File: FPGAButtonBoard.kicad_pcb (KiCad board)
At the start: 2 copper layers, 121.3 x 83.2 mm, 66 parts, among them J1 Conn_02x20_Odd_Even, J2 Analog Discovery 2, SW1 SW_DIP_x08, SW2 SW_DIP_x08, SW3 SW_Push, SW4 SW_Push, SW5 SW_Push, SW6 SW_Push, SW7 SW_Push, SW8 SW_SPST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

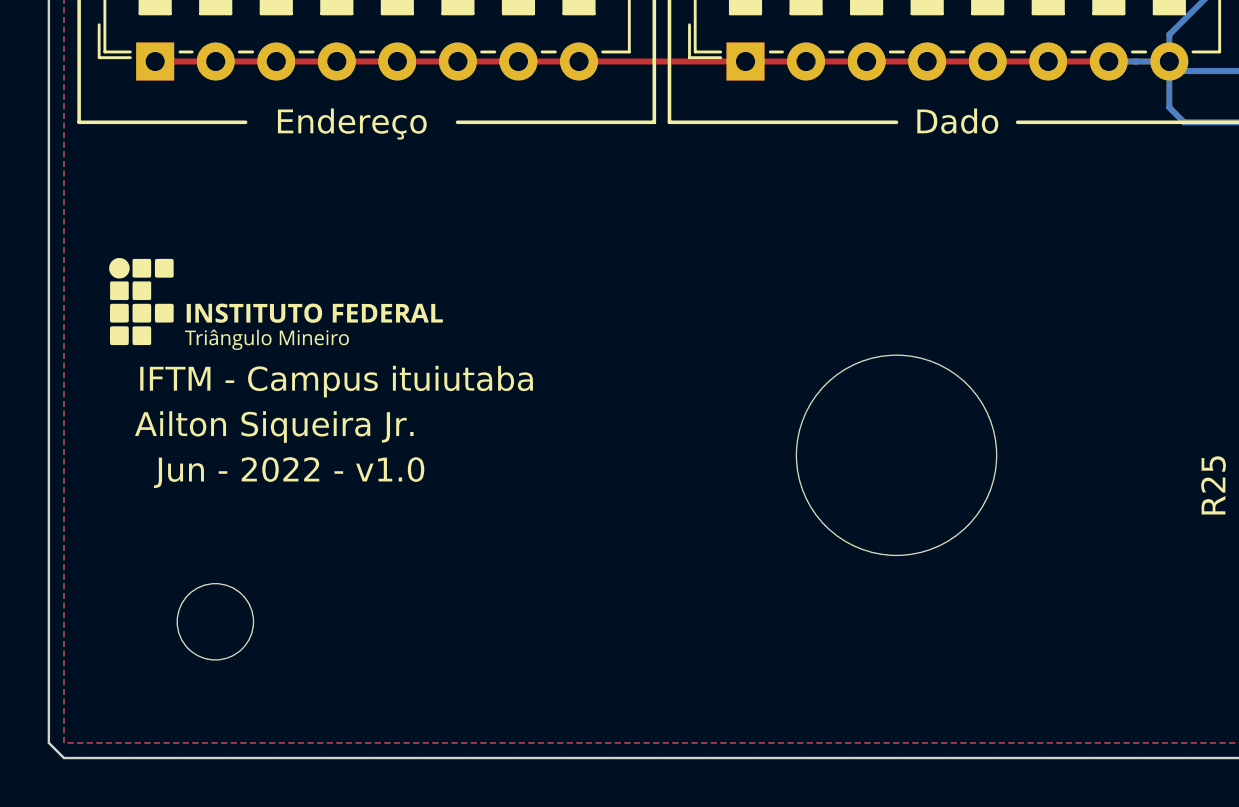
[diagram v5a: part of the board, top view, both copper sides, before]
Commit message: Adicionadas anotações dos pinos na placa.
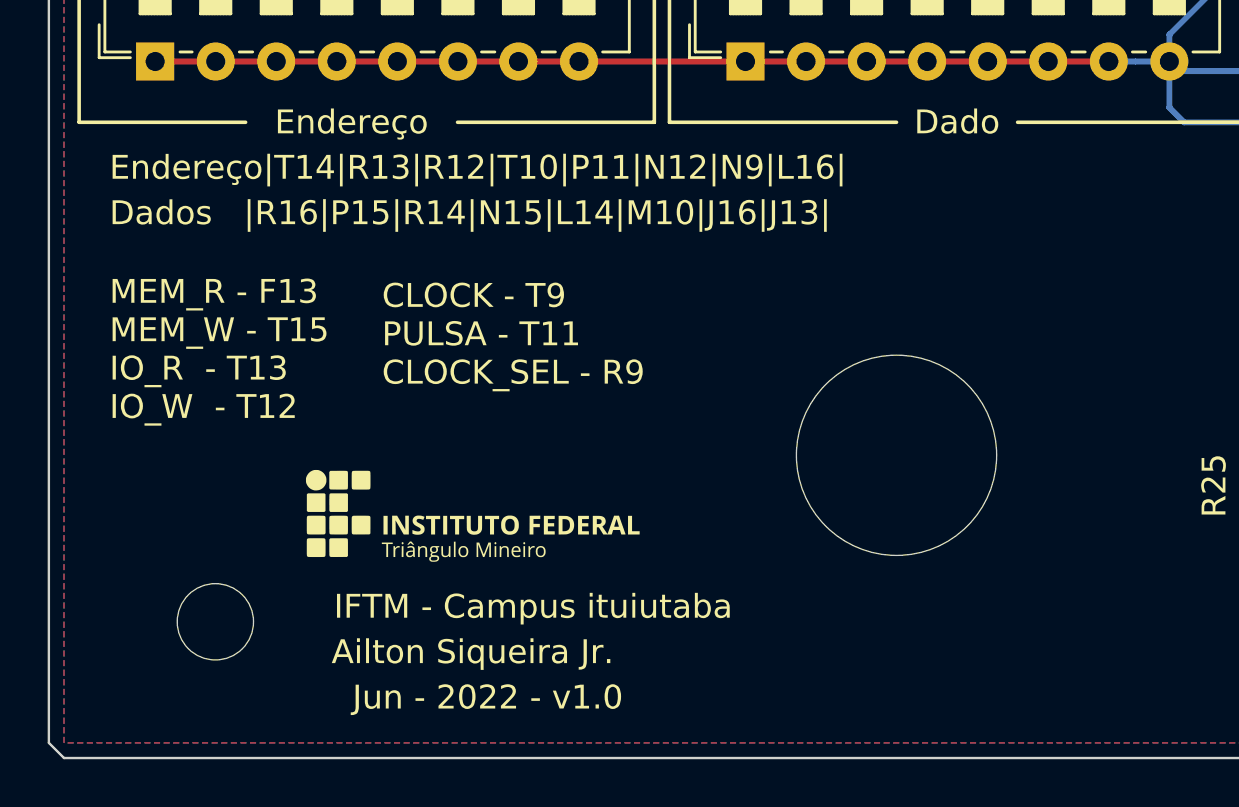
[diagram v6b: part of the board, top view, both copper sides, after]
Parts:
- moved G*** 12.1 mm to (108.0, 128.3)
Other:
- board text added: "CLOCK - T9 PULSA - T11 CLOCK_SEL - R9"
- board text added: "Dados |R16|P15|R14|N15|L14|M10|J16|J13|"
- board text added: "Endereço|T14|R13|R12|T10|P11|N12|N9|L16|"
- board text added: "MEM_R - F13 MEM_W - T15 IO_R - T13 IO_W - T12"
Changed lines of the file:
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@@
   )
   (footprint "Logo:IFTMLogoHor" (layer "F.Cu")
-    (at 99.695 119.38)
+    (at 107.95 128.27)
     (attr board_only exclude_from_pos_files exclude_from_bom)
     (fp_text reference "G***" (at 0 -2.54) (layer "F.SilkS") hide
@@
     (effects (font (size 1 1) (thickness 0.15)))
   )
-  (gr_text "Ailton Siqueira Jr." (at 99.695 124.46) (layer "F.SilkS")
+  (gr_text "Ailton Siqueira Jr." (at 107.95 133.985) (layer "F.SilkS")
     (effects (font (size 1 1) (thickness 0.15)))
+  )
+  (gr_text "Dados   |R16|P15|R14|N15|L14|M10|J16|J13|" (at 92.71 115.57) (layer "F.SilkS")
+    (effects (font (size 1 1) (thickness 0.15)) (justify left))
+  )
+  (gr_text "Endereço|T14|R13|R12|T10|P11|N12|N9|L16|" (at 92.71 113.665) (layer "F.SilkS")
+    (effects (font (size 1 1) (thickness 0.15)) (justify left))
   )
   (gr_text "MEM_R" (at 170.18 105.41) (layer "F.SilkS")
     (effects (font (size 1 1) (thickness 0.15)))
   )
-  (gr_text "Jun - 2022 - v1.0" (at 100.33 126.365) (layer "F.SilkS")
+  (gr_text "Jun - 2022 - v1.0" (at 108.585 135.89) (layer "F.SilkS")
     (effects (font (size 1 1) (thickness 0.15)))
   )
@@
     (effects (font (size 1 1) (thickness 0.15)))
   )
+  (gr_text "CLOCK - T9\nPULSA - T11\nCLOCK_SEL - R9" (at 104.14 120.65) (layer "F.SilkS")
+    (effects (font (size 1 1) (thickness 0.15)) (justify left))
+  )
   (gr_text "Pulsa" (at 193.04 134.62) (layer "F.SilkS")
     (effects (font (size 1 1) (thickness 0.15)))
+  )
+  (gr_text "MEM_R - F13\nMEM_W - T15\nIO_R  - T13\nIO_W  - T12\n" (at 92.71 121.285) (layer "F.SilkS")
+    (effects (font (size 1 1) (thickness 0.15)) (justify left))
   )
   (gr_text "Ajuste de Freq." (at 175.895 135.89) (layer "F.SilkS")
     (effects (font (size 1 1) (thickness 0.15)))
   )
-  (gr_text "IFTM - Campus ituiutaba" (at 102.235 122.555) (layer "F.SilkS")
+  (gr_text "IFTM - Campus ituiutaba" (at 110.49 132.08) (layer "F.SilkS")
     (effects (font (size 1 1) (thickness 0.15)))
   )

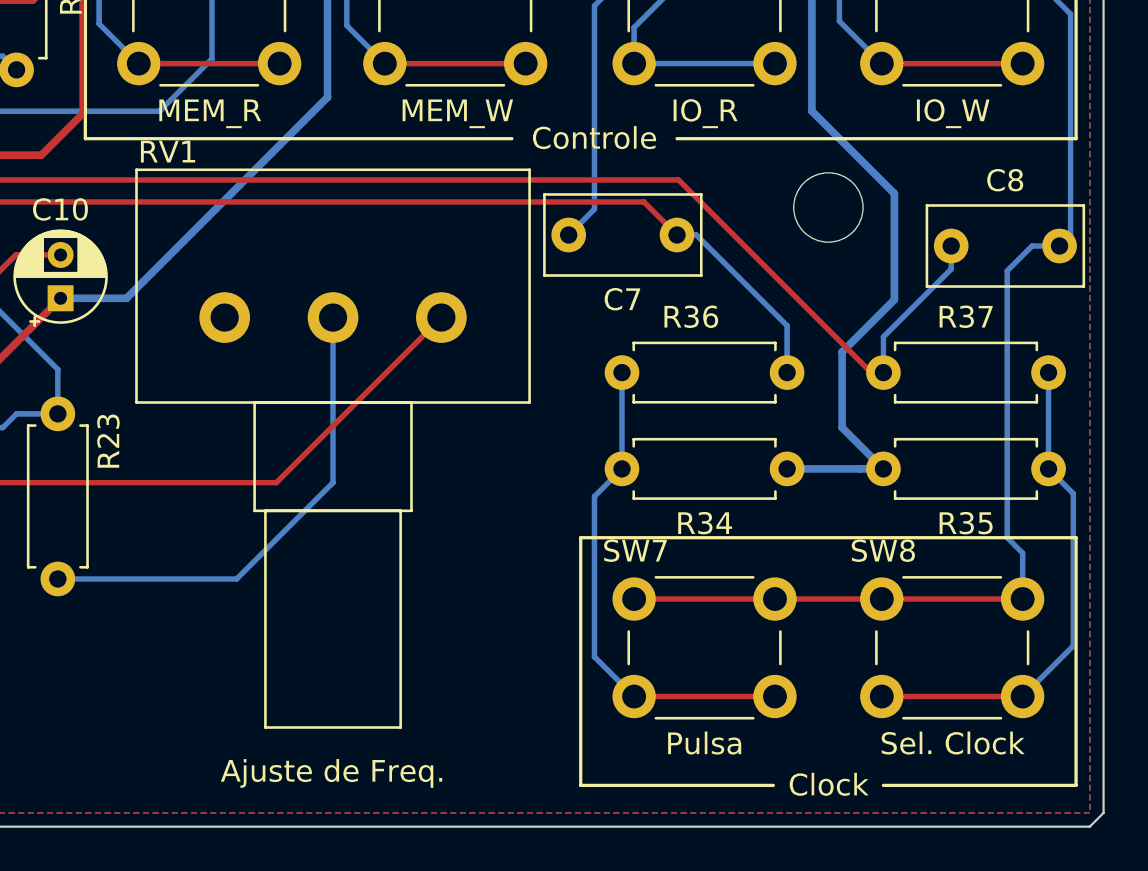
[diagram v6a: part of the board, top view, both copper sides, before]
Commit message: Corrigido o botão de seleção de Clock e valores dos capacitores.
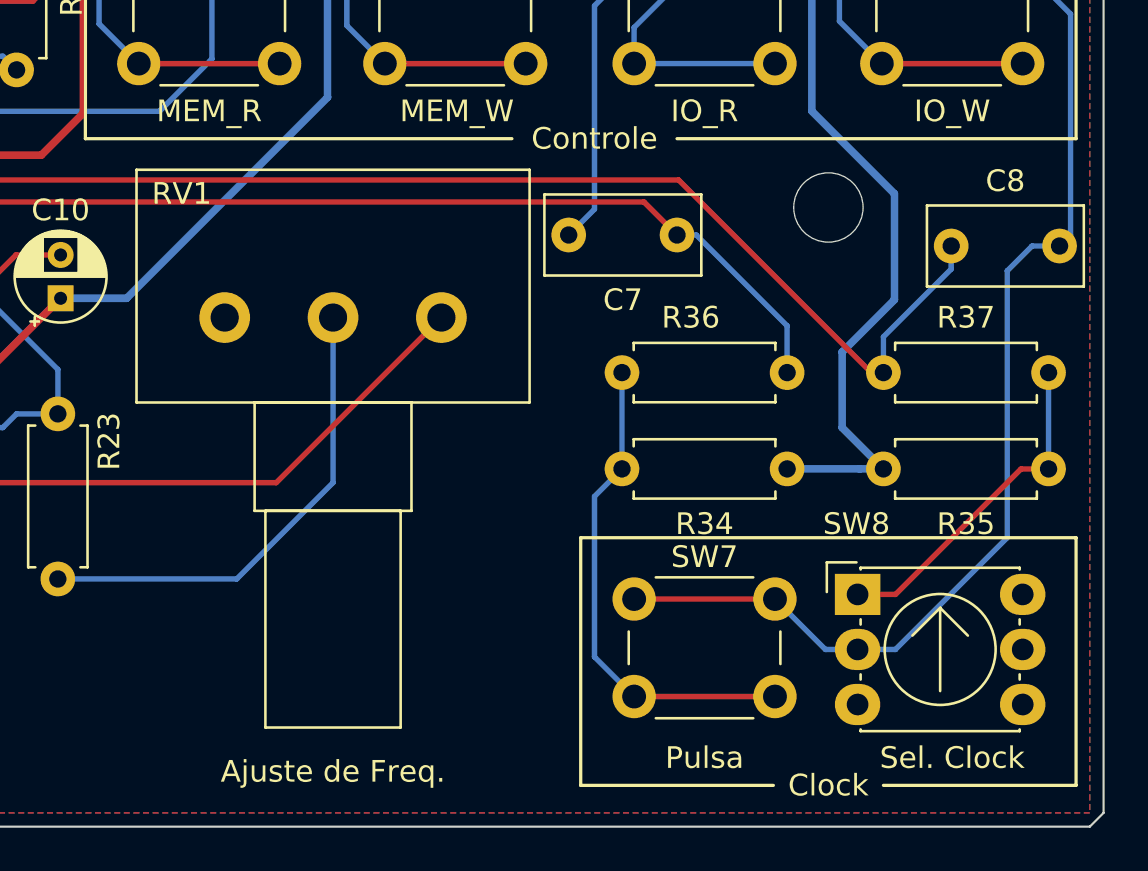
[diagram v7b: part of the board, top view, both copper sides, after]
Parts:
- C3, C4, C5, C6, C7, C8: value 100nF -> 47nF
- SW8: value SW_SPST -> SW_Push_DPDT; footprint Button_Switch_THT:SW_PUSH_6mm -> Logo:Nidec_Copal_SH-7010C_Mod
- moved SW8 1.14 mm to (200.1, 127.7)
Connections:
- SW8 pad 1: GND -> /DebounceCircuit3/SW_IN_6
- SW8 pad 2: /DebounceCircuit3/SW_IN_6 -> GND
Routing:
- net /DebounceCircuit3/SW_IN_6: track 22.9 -> 15.7 mm
- net GND: track 385.9 -> 385.1 mm

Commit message: Atualizado os valores dos capacitores
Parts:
- C1: value 10uF -> 47uF
- C3, C4, C5, C6, C7, C8: value 47nF -> 100nF
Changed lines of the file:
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@@
       (layerselection 0x00010fc_ffffffff)
       (disableapertmacros false)
-      (usegerberextensions false)
+      (usegerberextensions true)
       (usegerberattributes true)
-      (usegerberadvancedattributes true)
-      (creategerberjobfile true)
+      (usegerberadvancedattributes false)
+      (creategerberjobfile false)
       (svguseinch false)
       (svgprecision 6)
@@
       (psa4output false)
       (plotreference true)
-      (plotvalue true)
+      (plotvalue false)
       (plotinvisibletext false)
       (sketchpadsonfab false)
-      (subtractmaskfromsilk false)
+      (subtractmaskfromsilk true)
       (outputformat 1)
       (mirror false)
-      (drillshape 1)
+      (drillshape 0)
       (scaleselection 1)
-      (outputdirectory "")
+      (outputdirectory "Gerber/")
     )
   )
@@
       (effects (font (size 1 1) (thickness 0.15)))
     )
-    (fp_text value "10uF" (at -1.5674 0) (layer "F.Fab")
+    (fp_text value "47uF" (at -1.5674 0) (layer "F.Fab")
       (effects (font (size 1 1) (thickness 0.15)))
     )
@@
       (effects (font (size 1 1) (thickness 0.15)))
     )
-    (fp_text value "47nF" (at 2.5 3) (layer "F.Fab")
+    (fp_text value "100nF" (at 2.5 3) (layer "F.Fab")
       (effects (font (size 1 1) (thickness 0.15)))
     )
@@
       (effects (font (size 1 1) (thickness 0.15)))
     )
-    (fp_text value "47nF" (at 2.5 3) (layer "F.Fab")
+    (fp_text value "100nF" (at 2.5 3) (layer "F.Fab")
       (effects (font (size 1 1) (thickness 0.15)))
     )
@@
       (effects (font (size 1 1) (thickness 0.15)))
     )
-    (fp_text value "47nF" (at 2.5 3) (layer "F.Fab")
+    (fp_text value "100nF" (at 2.5 3) (layer "F.Fab")
       (effects (font (size 1 1) (thickness 0.15)))
     )
@@
     (fp_line (start 5.72 -5.1) (end 5.72 40.66) (layer "F.Fab") (width 0.1))
     (fp_line (start -1.98 -3.91) (end 4.52 -3.91) (layer "F.Fab") (width 0.1))
-    (pad "1" thru_hole roundrect (at 0 0 90) (size 1.7 1.7) (drill 1) (layers *.Cu *.Mask) (roundrect_rratio 0.147059)
+    (pad "1" thru_hole roundrect (at 0 0 90) (size 1.7 1.7) (drill 1) (layers *.Cu *.Mask) (roundrect_rratio 0.1470588235)
       (net 30 "/D7") (pinfunction "Pin_1") (pintype "passive"))
     (pad "2" thru_hole circle (at 2.54 0 90) (size 1.7 1.7) (drill 1) (layers *.Cu *.Mask)
@@
       (effects (font (size 1 1) (thickness 0.15)))
     )
-    (fp_text value "47nF" (at 2.5 3 180) (layer "F.Fab")
+    (fp_text value "100nF" (at 2.5 3 180) (layer "F.Fab")
       (effects (font (size 1 1) (thickness 0.15)))
     )
@@
       (effects (font (size 1 1) (thickness 0.15)))
     )
-    (fp_text value "47nF" (at 2.5 3) (layer "F.Fab")
+    (fp_text value "100nF" (at 2.5 3) (layer "F.Fab")
       (effects (font (size 1 1) (thickness 0.15)))
     )
@@
       (effects (font (size 1 1) (thickness 0.15)))
     )
-    (fp_text value "47nF" (at 2.5 3) (layer "F.Fab")
+    (fp_text value "100nF" (at 2.5 3) (layer "F.Fab")
       (effects (font (size 1 1) (thickness 0.15)))
     )
